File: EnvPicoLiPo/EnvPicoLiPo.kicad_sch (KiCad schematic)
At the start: 72 parts, among them J2 SKRKAEE020, J3 2.54mm header 01x20, J4 2.54mm header 01x20, J5 Conn_01x03_Male, U1 LM3671MF 3.3, U2 BQ24072RGT, U3 RP2040, U4 ESP32-PICO-D4, X1 XO 32 12Mhz 3225 seiko

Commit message: Corrected all the via placements so they dont cause issues and removed some redundant parts
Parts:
- removed C12: 0.1uf 0402, Capacitor_SMD:C_0402_1005Metric, symbol Device:C_Small
- removed C4: 1uf 0402, Capacitor_SMD:C_0402_1005Metric, symbol Device:C
- removed D1: 0402 led, LED_SMD:LED_0402_1005Metric, symbol Device:LED_Small
- removed R13: 2.2K 0402, Resistor_SMD:R_0402_1005Metric, symbol Device:R_Small
- D4: value Schottky 0603 -> 1n4002 0603
- R7: value 100ohm -> 100k 0402
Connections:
- net VSYS: no longer U2.6 (EN1)
- net VBAT: now reaches BT1.1 (+), C21.2, U2.2 (BAT), U2.3 (BAT)
- net VBAT: now also U2.6 (EN1)
- no-connect marks 2 -> 3
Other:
- note added: "D1 NEEDS to be 0omh resistor or 1n4002"
- note added: "MAKE SURE THIS LINE is ran off close to pin43"
- note removed: "D1 NEEDS to be 0omh resistor or schotky resistor"
- note removed: "MAKE SURE THIS LINE is ran off of pin43"
- moved on the sheet: C9

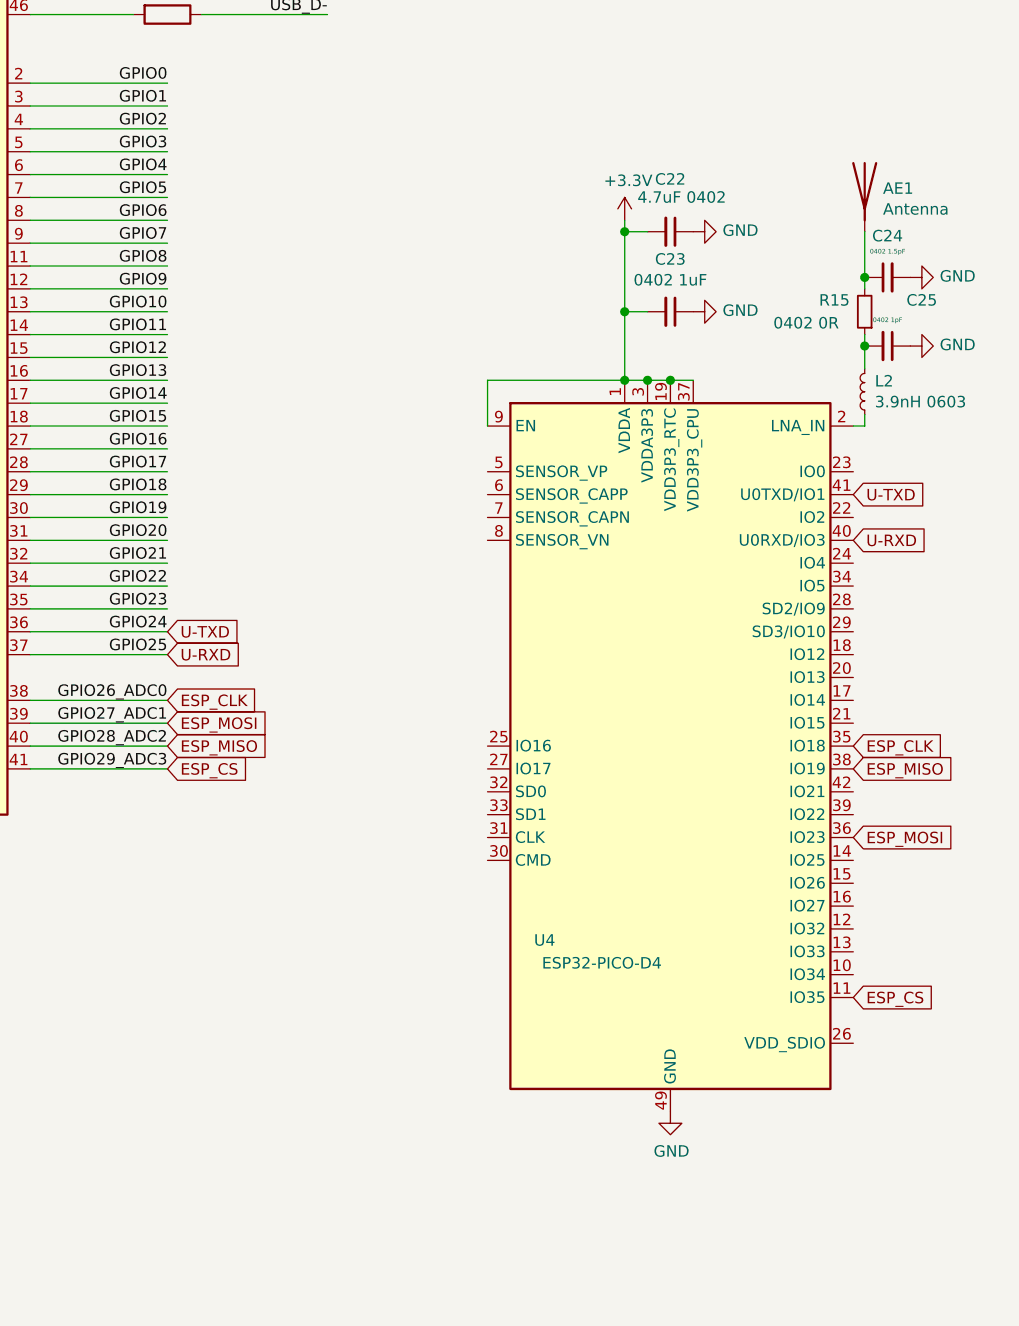
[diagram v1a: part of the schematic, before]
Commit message: removed ESP32 and wifi bits for now, will re-add something later on with further testing.
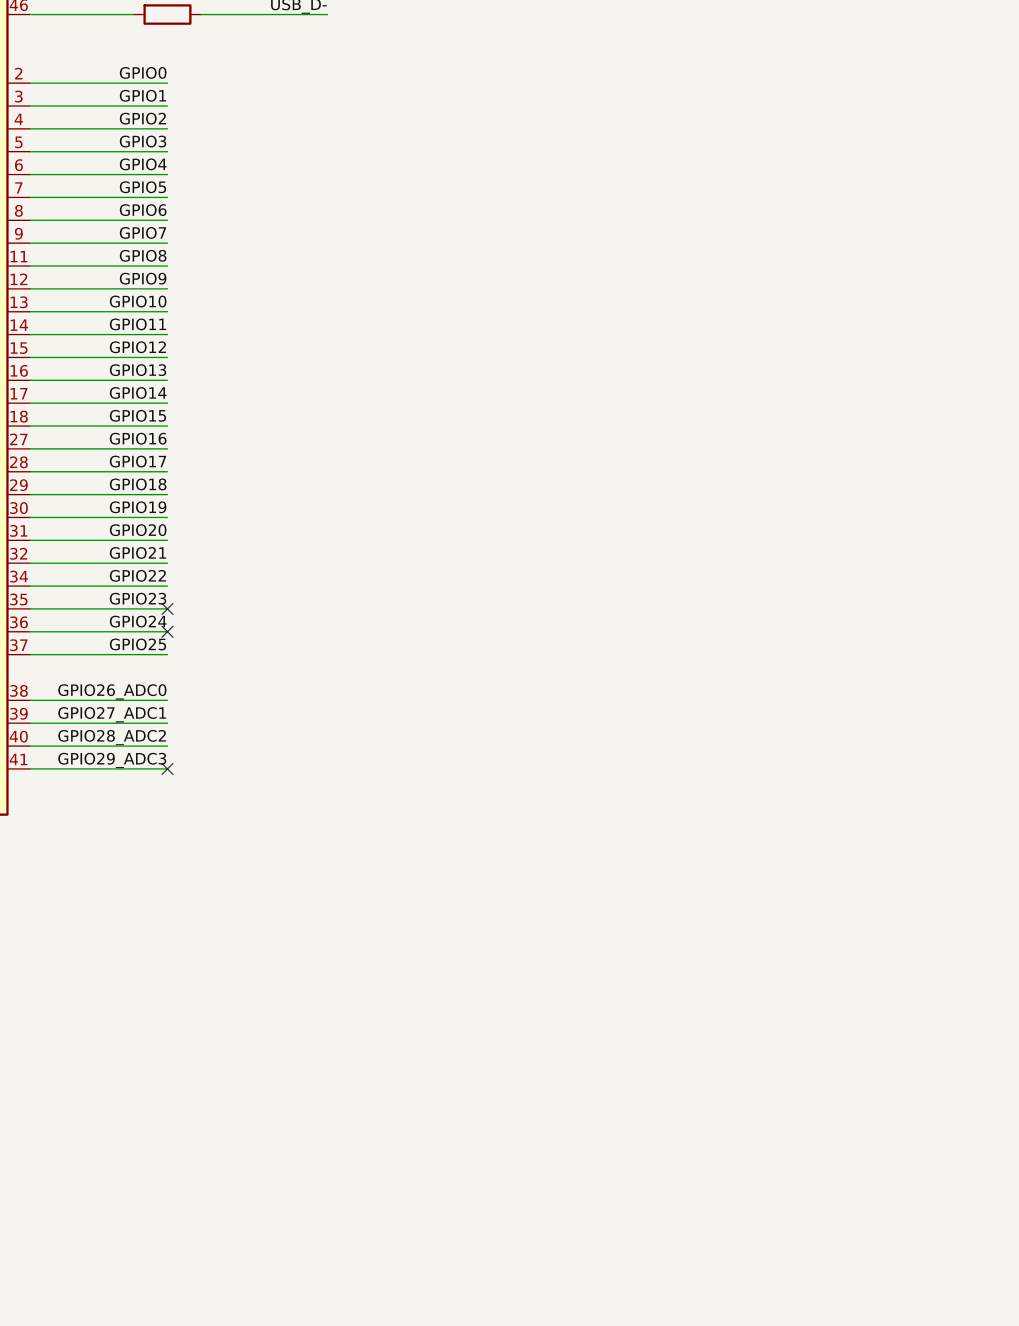
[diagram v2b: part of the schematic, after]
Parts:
- removed AE1: Antenna, RF_Antenna:Texas_SWRA117D_2.4GHz_Left, symbol Device:Antenna
- removed C22: 4.7uF 0402, Capacitor_SMD:C_0402_1005Metric, symbol Device:C_Small
- removed C23: 0402 1uF, Capacitor_SMD:C_0402_1005Metric, symbol Device:C_Small
- removed C24: 0402 1.5pF, Capacitor_SMD:C_0402_1005Metric, symbol Device:C_Small
- removed C25: 0402 1pF, Capacitor_SMD:C_0402_1005Metric, symbol Device:C_Small
- removed L2: 3.9nH 0603, Inductor_SMD:L_0603_1608Metric, symbol Device:L_Small
- removed R15: 0402 0R, Resistor_SMD:R_0402_1005Metric, symbol Device:R_Small
- removed U4: ESP32-PICO-D4, Package_DFN_QFN:QFN-48-1EP_7x7mm_P0.5mm_EP5.3x5.3mm, symbol RF_Module:ESP32-PICO-D4
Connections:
- net ESP_CLK renamed GPIO26_ADC0
- net ESP_CS renamed GPIO29_ADC3
- net ESP_MISO renamed GPIO28_ADC2
- net ESP_MOSI renamed GPIO27_ADC1
- net U-RXD renamed GPIO25
- net U-TXD renamed GPIO24
- no-connect marks 3 -> 6

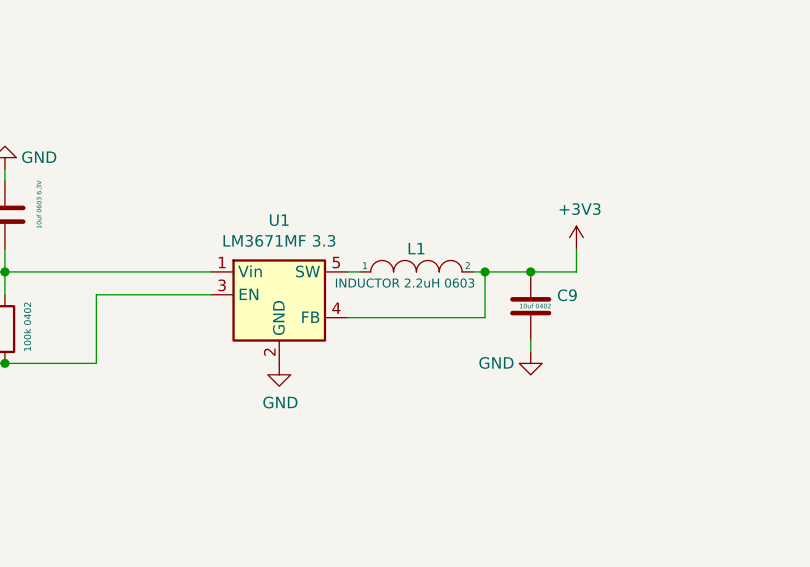
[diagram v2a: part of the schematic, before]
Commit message: moved the battery connector to the bottom of the board and rotated the debug header 90 degrees to fit along side.
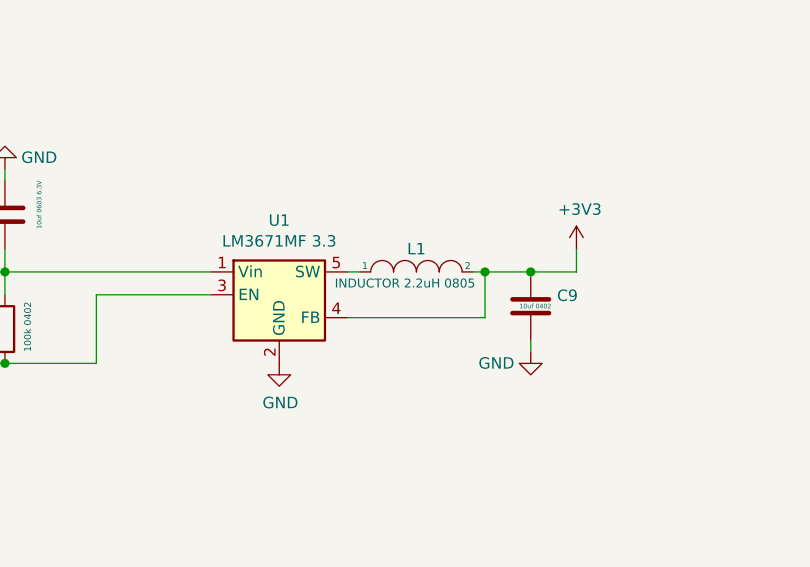
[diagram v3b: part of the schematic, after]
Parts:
- BT1: footprint Connector_JST:JST_PH_B2B-PH-K_1x02_P2.00mm_Vertical -> Connector_JST:JST_PH_B2B-PH-SM4-TB_1x02-1MP_P2.00mm_Vertical
- L1: value INDUCTOR 2.2uH 0603 -> INDUCTOR 2.2uH 0805; footprint Inductor_SMD:L_0603_1608Metric -> Inductor_SMD:L_0805_2012Metric
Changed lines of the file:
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@@
     (in_bom yes) (on_board yes)
     (property "Reference" "L1" (id 0) (at 217.17 44.45 0))
-    (property "Value" "INDUCTOR 2.2uH 0603" (id 1) (at 215.9 48.26 0)
+    (property "Value" "INDUCTOR 2.2uH 0805" (id 1) (at 215.9 48.26 0)
       (effects (font (size 0.9906 0.9906)))
     )
-    (property "Footprint" "Inductor_SMD:L_0603_1608Metric" (id 2) (at 217.17 46.99 0)
+    (property "Footprint" "Inductor_SMD:L_0805_2012Metric" (id 2) (at 217.17 46.99 0)
       (effects (font (size 1.27 1.27)) hide)
     )
@@
       (effects (font (size 0.508 0.508)) (justify left))
     )
-    (property "Footprint" "Connector_JST:JST_PH_B2B-PH-K_1x02_P2.00mm_Vertical" (id 2) (at 133.096 46.99 90)
+    (property "Footprint" "Connector_JST:JST_PH_B2B-PH-SM4-TB_1x02-1MP_P2.00mm_Vertical" (id 2) (at 133.096 46.99 90)
       (effects (font (size 1.27 1.27)) hide)
     )
@@
     )
     (path "/00000000-0000-0000-0000-000061185e74"
-      (reference "BT1") (unit 1) (value "Li-Po Battery") (footprint "Connector_JST:JST_PH_B2B-PH-K_1x02_P2.00mm_Vertical")
+      (reference "BT1") (unit 1) (value "Li-Po Battery") (footprint "Connector_JST:JST_PH_B2B-PH-SM4-TB_1x02-1MP_P2.00mm_Vertical")
     )
     (path "/00000000-0000-0000-0000-00005f09255d"
@@
     )
     (path "/00000000-0000-0000-0000-00006114ddae"
-      (reference "L1") (unit 1) (value "INDUCTOR 2.2uH 0603") (footprint "Inductor_SMD:L_0603_1608Metric")
+      (reference "L1") (unit 1) (value "INDUCTOR 2.2uH 0805") (footprint "Inductor_SMD:L_0805_2012Metric")
     )
     (path "/00000000-0000-0000-0000-0000612459f2"

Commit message: changed JST connector for more common type, adjusted some parts to do with flash
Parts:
- removed X1: XO 32 12Mhz 3225 seiko, Crystal:Crystal_SMD_SeikoEpson_TSX3225-4Pin_3.2x2.5mm, symbol Oscillator:XO32
- added C19: 15pf 0402, Capacitor_SMD:C_0402_1005Metric, symbol Device:C
- added Y1: Crystal_GND24 12MHz, Crystal:Crystal_SMD_3225-4Pin_3.2x2.5mm, symbol Device:Crystal_GND24
- BT1: footprint Connector_JST:JST_PH_B2B-PH-SM4-TB_1x02-1MP_P2.00mm_Vertical -> Connector_JST:JST_XH_B2B-XH-A_1x02_P2.50mm_Vertical
- R11: renamed from R2; value DNF -> 10K 0402
- renumbered C19 to C1, C13 to C10, C14 to C11, C15 to C12, C16 to C13, C18 to C14, C10 to C15, C3 to C16, C5 to C17, C2 to C18, C20 to C2, C17 to C20, C1 to C3, C21 to C4, C9 to C5, C11 to C8, C8 to C9, D4 to D1, J2 to J1, J3 to J2, J4 to J3, J5 to J4, R5 to R1, R4 to R10, R1 to R12, R8 to R13, R12 to R2, R6 to R3, R7 to R4, R9 to R5, R14 to R6, R11 to R7, R10 to R8, R3 to R9, TP7 to TP6, TP6 to TP7, U2 to U1, U1 to U2
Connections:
- net GND: now also C19.1, Y1.2, Y1.4
- net XIN: now also Y1.3
- net XOUT: now also C19.2, Y1.1
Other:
- note removed: "Dont bother trying to use a crystal as it massively complicates this clock source setup"
- note removed: "Intentionally left floating"
- note removed: "Pin1 on XO Oscillator also left floating so the chip is enabled (this is specified in their datasheet)"
- note removed: "Use a 12mhz Seiko Oscilator, 3225-4Pin"
- moved on the sheet: C18
